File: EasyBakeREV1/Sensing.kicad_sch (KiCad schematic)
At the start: 18 parts, among them U7 MAX31855_SO8, U8 LM324

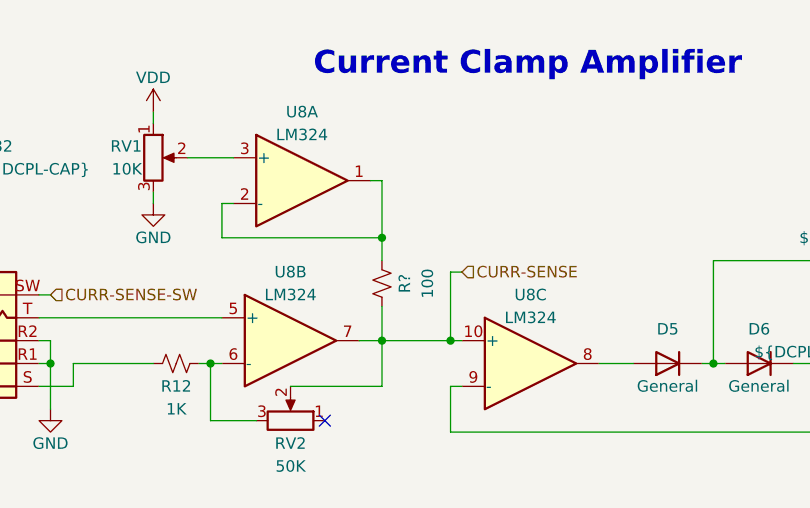
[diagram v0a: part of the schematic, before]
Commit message: REV3 - Reorganize MC pinouts and add LED driver (WIP)
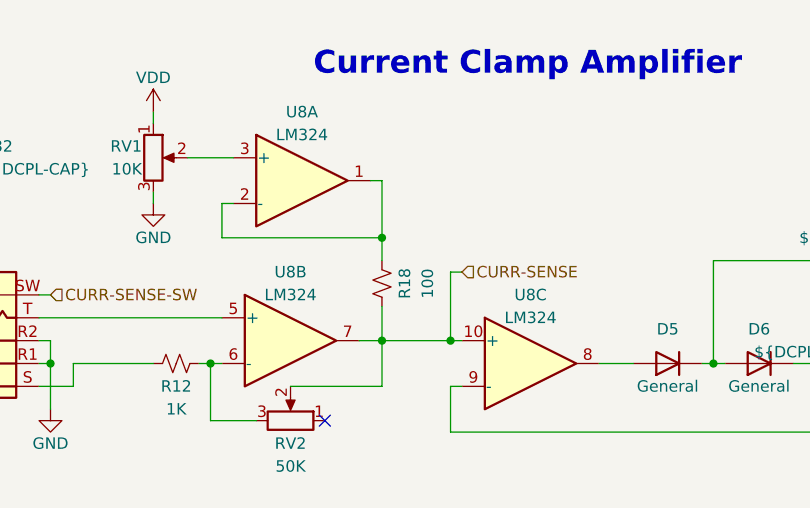
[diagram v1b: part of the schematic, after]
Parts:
- gave numbers to parts that had none: 1
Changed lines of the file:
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@@
   (symbol (lib_id "Device:R_Small_US") (at 148.59 116.84 180) (unit 1)
     (in_bom yes) (on_board yes)
-    (property "Reference" "R?" (id 0) (at 151.13 116.84 90))
+    (property "Reference" "R18" (id 0) (at 151.13 116.84 90))
     (property "Value" "100" (id 1) (at 153.67 116.84 90))
     (property "Footprint" "Resistor_SMD:R_0603_1608Metric" (id 2) (at 148.59 116.84 0)

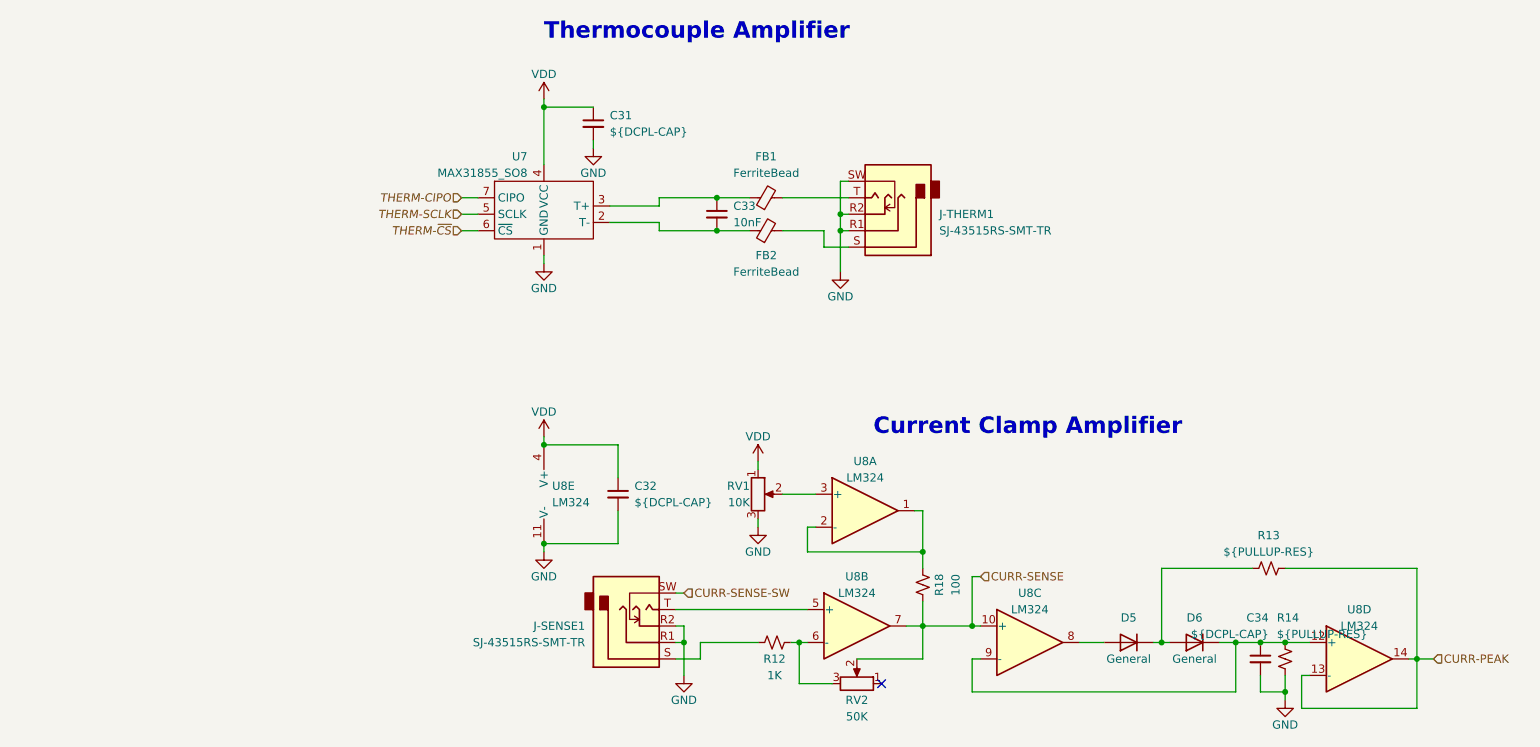
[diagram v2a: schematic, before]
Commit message: Change main pwr to 3.3 due to USB issues
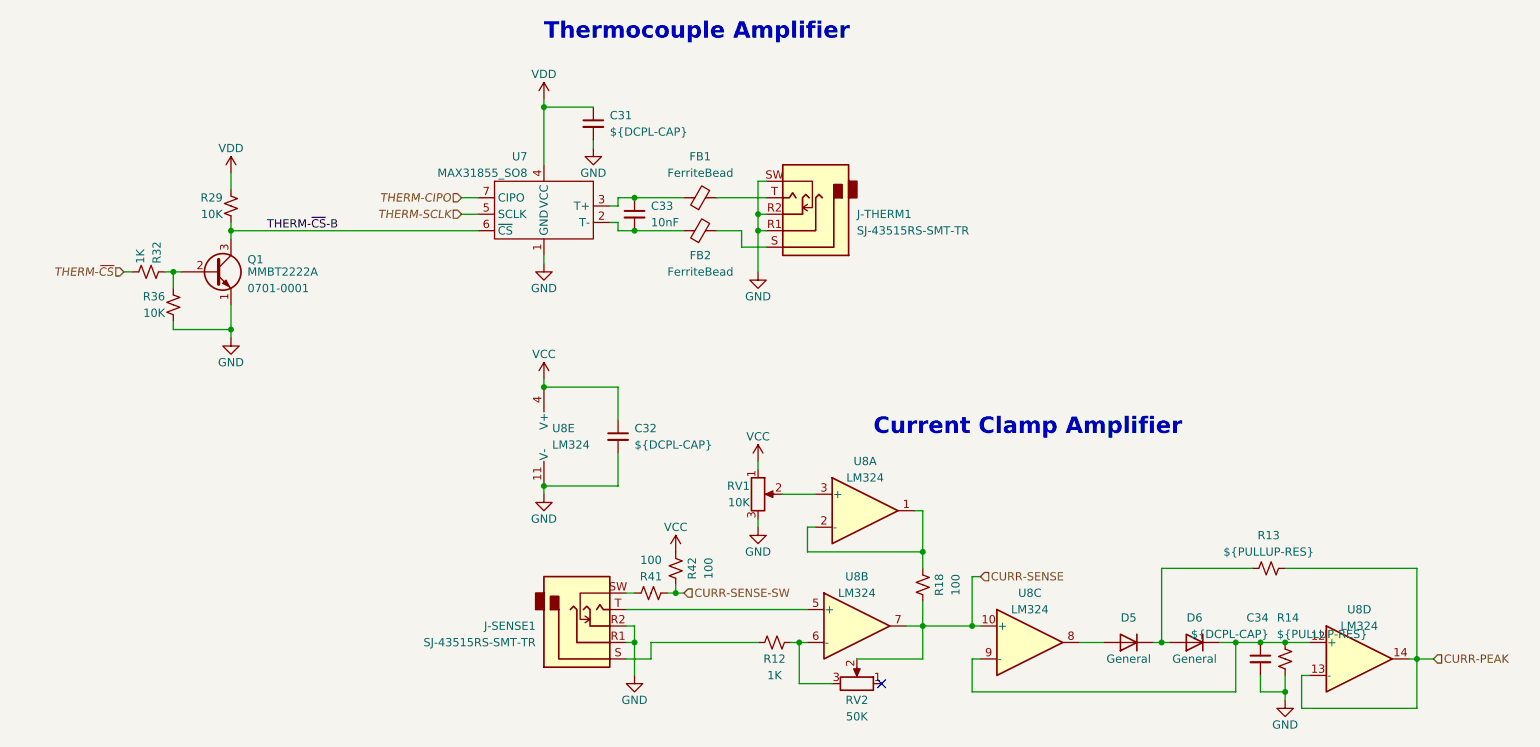
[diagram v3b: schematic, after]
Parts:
- added Q1: MMBT2222A, Package_TO_SOT_SMD:SOT-23, symbol Daxxn_Transistors:MMBT2222A
- added R29, R36: 10K, Resistor_SMD:R_0603_1608Metric, symbol Device:R_Small_US
- added R32: 1K, Resistor_SMD:R_0603_1608Metric, symbol Device:R_Small_US
- added R41, R42: 100, Resistor_SMD:R_0603_1608Metric, symbol Device:R_Small_US
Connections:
- net CURR-SENSE-SW: now also R41.1, R42.1; no longer J-SENSE1.SW
- net GND: now also Q1.1 (E), R36.2
- net THERM-~{CS}: now also R32.2; no longer U7.6 (~{CS})
- net VDD: now also R29.1; no longer C32.1, RV1.1, U8.4 (V+)
- new net: Q1.2 (B), R32.1, R36.1
- new net: J-SENSE1.SW, R41.2
- new net THERM-~{CS}-B: Q1.3 (C), R29.2, U7.6 (~{CS})
- new net VCC: C32.1, R42.2, RV1.1, U8.4 (V+)
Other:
- moved on the sheet: C32, C33, FB1, FB2, J-SENSE1, J-THERM1, U8E

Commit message: Replaced MCU - started layout
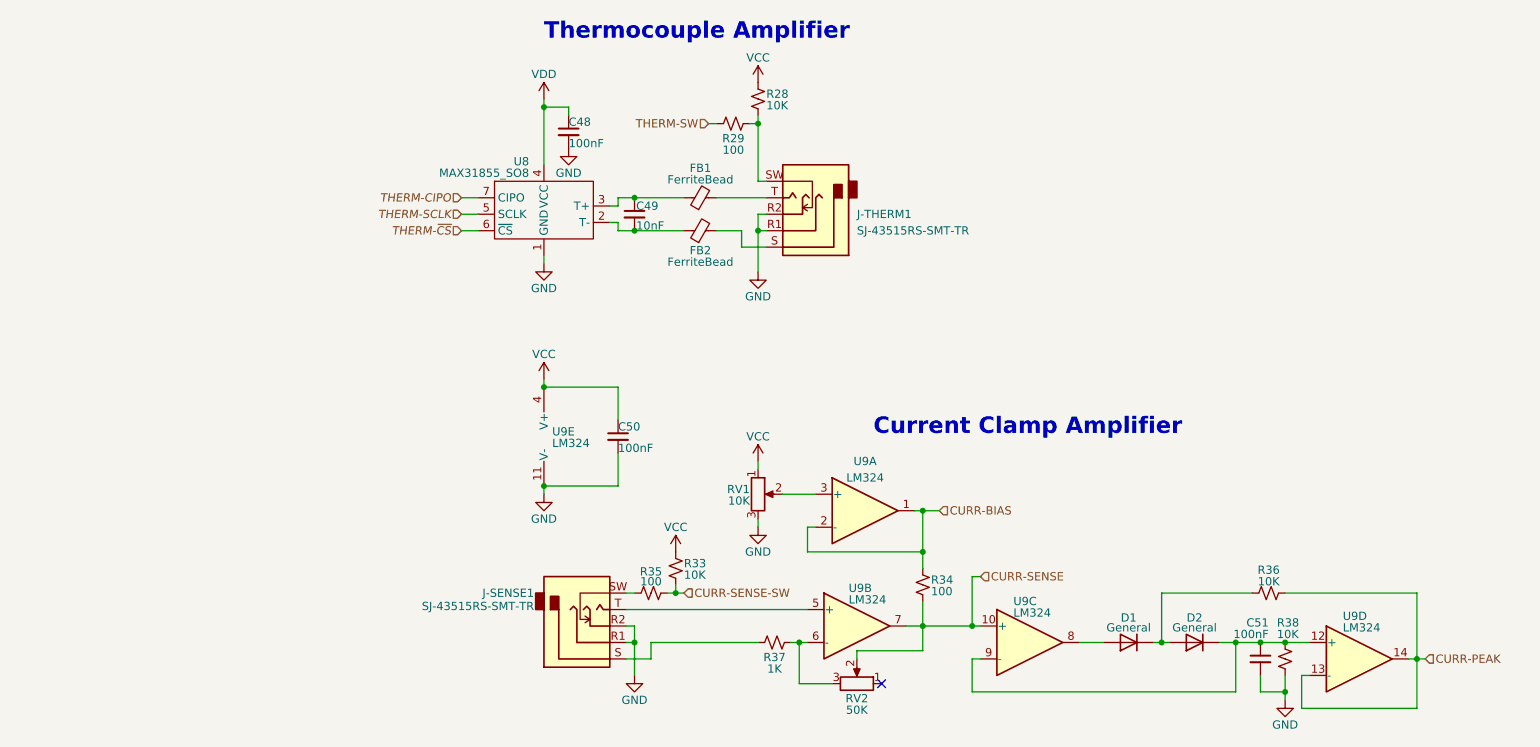
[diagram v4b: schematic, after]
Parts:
- removed Q1: MMBT2222A, Package_TO_SOT_SMD:SOT-23, symbol Daxxn_Transistors:MMBT2222A
- removed R32: 1K, Resistor_SMD:R_0603_1608Metric, symbol Device:R_Small_US
- removed R36: 10K, Resistor_SMD:R_0603_1608Metric, symbol Device:R_Small_US
- added R28: 10K, Resistor_SMD:R_0402_1005Metric, symbol Device:R_Small_US
- C48: renamed from C31; value ${DCPL-CAP} -> 100nF; footprint Capacitor_SMD:C_0603_1608Metric -> Capacitor_SMD:C_0402_1005Metric
- C49: renamed from C33; footprint Capacitor_SMD:C_0603_1608Metric -> Capacitor_SMD:C_0402_1005Metric
- C50: renamed from C32; value ${DCPL-CAP} -> 100nF; footprint Capacitor_SMD:C_0603_1608Metric -> Capacitor_SMD:C_0402_1005Metric
- C51: renamed from C34; value ${DCPL-CAP} -> 100nF; footprint Capacitor_SMD:C_0603_1608Metric -> Capacitor_SMD:C_0402_1005Metric
- R29: value 10K -> 100; footprint Resistor_SMD:R_0603_1608Metric -> Resistor_SMD:R_0402_1005Metric
- R33: renamed from R42; value 100 -> 10K; footprint Resistor_SMD:R_0603_1608Metric -> Resistor_SMD:R_0402_1005Metric
- R34: renamed from R18; footprint Resistor_SMD:R_0603_1608Metric -> Resistor_SMD:R_0402_1005Metric
- R35: renamed from R41; footprint Resistor_SMD:R_0603_1608Metric -> Resistor_SMD:R_0402_1005Metric
- R36: renamed from R13; value ${PULLUP-RES} -> 10K; footprint Resistor_SMD:R_0603_1608Metric -> Resistor_SMD:R_0402_1005Metric
- R37: renamed from R12; footprint Resistor_SMD:R_0603_1608Metric -> Resistor_SMD:R_0402_1005Metric
- R38: renamed from R14; value ${PULLUP-RES} -> 10K; footprint Resistor_SMD:R_0603_1608Metric -> Resistor_SMD:R_0402_1005Metric
- RV1, RV2: footprint Potentiometer_THT:Potentiometer_Bourns_3296W_Vertical -> Daxxn_Switches:Bourns_TC33X
- renumbered D5 to D1, D6 to D2, U7 to U8, U8 to U9
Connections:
- net GND: no longer J-THERM1.SW
- net THERM-~{CS}: now also U8.6 (~{CS})
- net VCC: now also R28.2
- net VDD: no longer R29.1
- net CURR-BIAS: now reaches R34.2, U9.1, U9.2 (-)
- net THERM-~{CS}-B renamed THERM-SW
- net THERM-SW: no longer U8.6 (~{CS})
- new net: J-THERM1.SW, R28.1, R29.1
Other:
- moved on the sheet: C48, R36

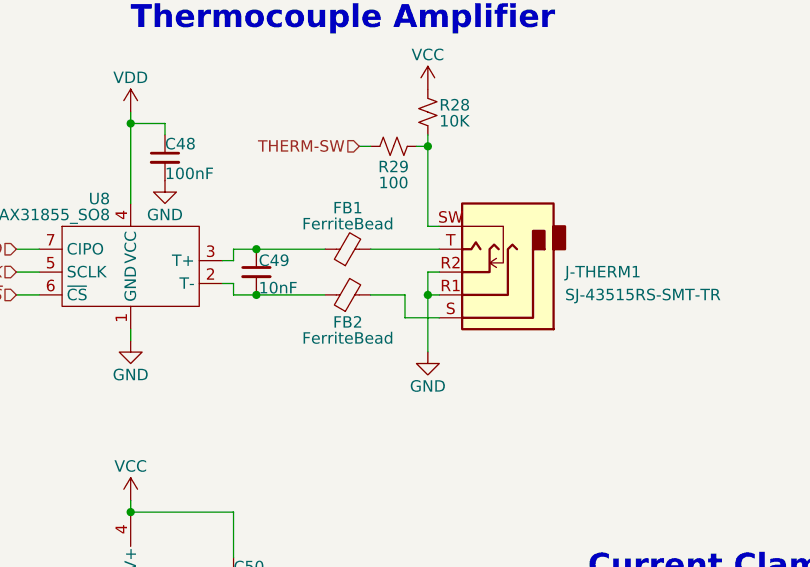
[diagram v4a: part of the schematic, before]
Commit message: Rearrange footprints and start layout
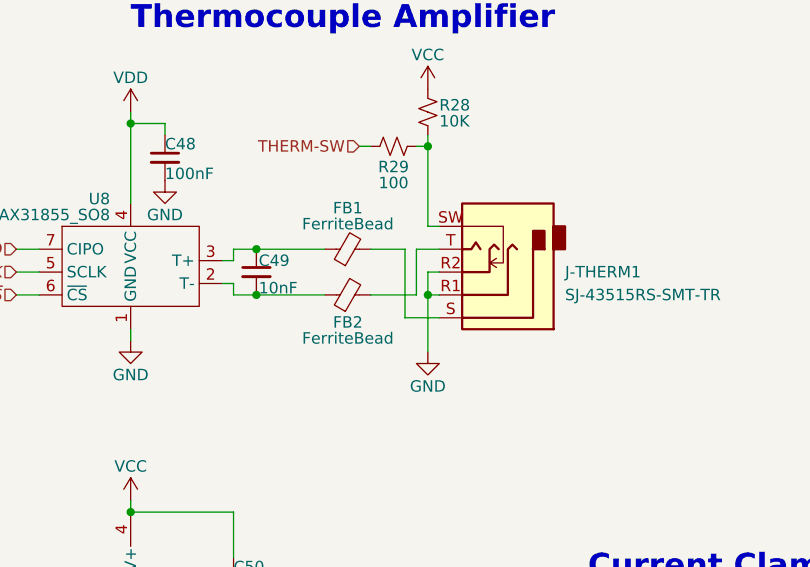
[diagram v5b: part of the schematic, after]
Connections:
- net at J-THERM1.S: now also FB1.2; no longer FB2.2
- net at J-THERM1.T: now also FB2.2; no longer FB1.2
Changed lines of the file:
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@@
+    (stroke (width 0) (type default))
+  )
+  (wire (pts (xy 120.65 57.15) (xy 120.65 64.77))
     (stroke (width 0) (type default))
   )
@@
   )
   (wire (pts (xy 130.81 107.95) (xy 132.08 107.95))
+    (stroke (width 0) (type default))
+  )
+  (wire (pts (xy 121.92 62.23) (xy 121.92 57.15))
     (stroke (width 0) (type default))
   )
@@
     (stroke (width 0) (type default))
   )
+  (wire (pts (xy 121.92 57.15) (xy 124.46 57.15))
+    (stroke (width 0) (type default))
+  )
   (wire (pts (xy 110.49 118.11) (xy 111.76 118.11))
+    (stroke (width 0) (type default))
+  )
+  (wire (pts (xy 120.65 64.77) (xy 124.46 64.77))
     (stroke (width 0) (type default))
   )
@@
     (stroke (width 0) (type default))
   )
+  (wire (pts (xy 116.84 57.15) (xy 120.65 57.15))
+    (stroke (width 0) (type default))
+  )
   (wire (pts (xy 77.47 62.23) (xy 80.01 62.23))
     (stroke (width 0) (type default))
   )
   (wire (pts (xy 110.49 116.84) (xy 110.49 118.11))
-    (stroke (width 0) (type default))
-  )
-  (wire (pts (xy 120.65 64.77) (xy 124.46 64.77))
     (stroke (width 0) (type default))
   )
@@
     (stroke (width 0) (type default))
   )
-  (wire (pts (xy 116.84 62.23) (xy 120.65 62.23))
+  (wire (pts (xy 116.84 62.23) (xy 121.92 62.23))
     (stroke (width 0) (type default))
   )
@@
     (stroke (width 0) (type default))
   )
-  (wire (pts (xy 116.84 57.15) (xy 124.46 57.15))
-    (stroke (width 0) (type default))
-  )
   (wire (pts (xy 148.59 111.76) (xy 130.81 111.76))
     (stroke (width 0) (type default))
   )
-  (wire (pts (xy 120.65 62.23) (xy 120.65 64.77))
-    (stroke (width 0) (type default))
-  )
